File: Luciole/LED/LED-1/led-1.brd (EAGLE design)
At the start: 29.9 x 29.3 mm, 19 parts, among them J1 LiPo, J2 USB-MICROB, Q1 2.5A/30V, U1 MCP73831, U2 3.3V

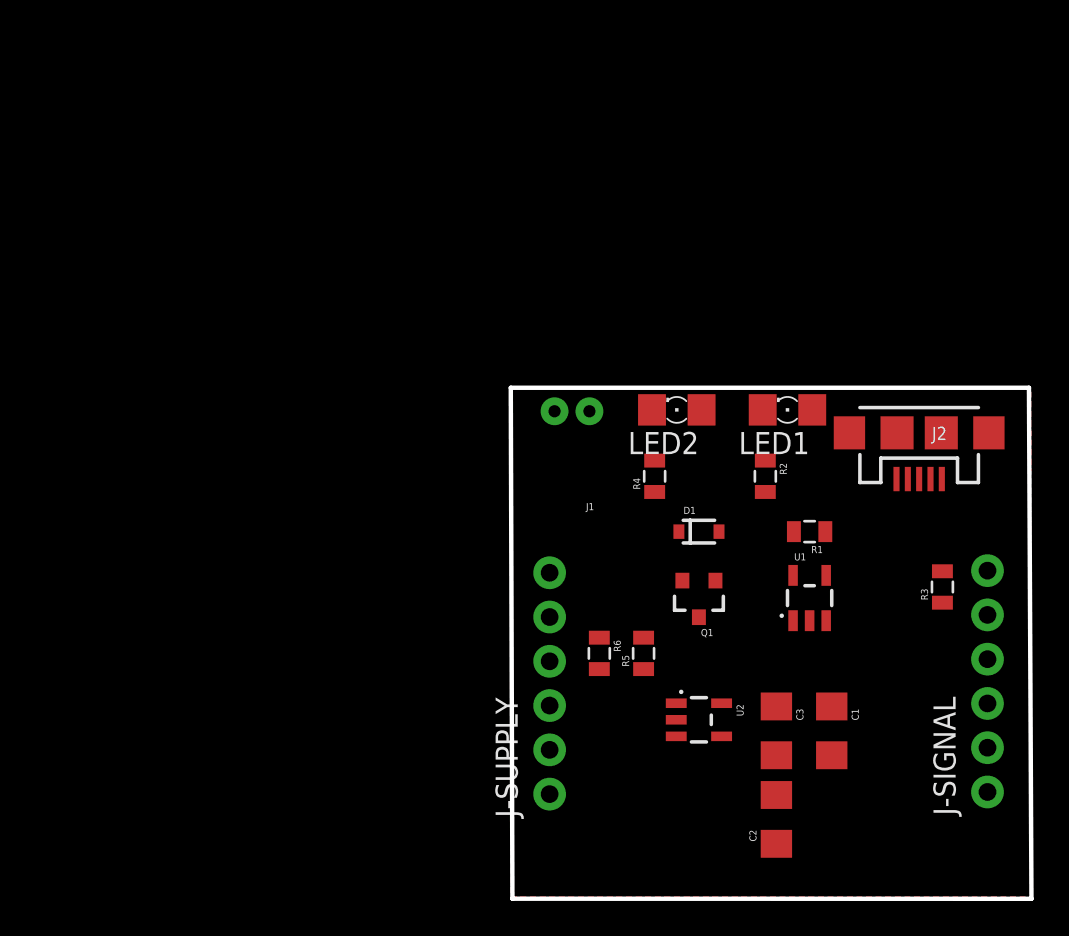
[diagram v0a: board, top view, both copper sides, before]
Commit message: Luciole V1 Ok ; Baballe V1 En cours
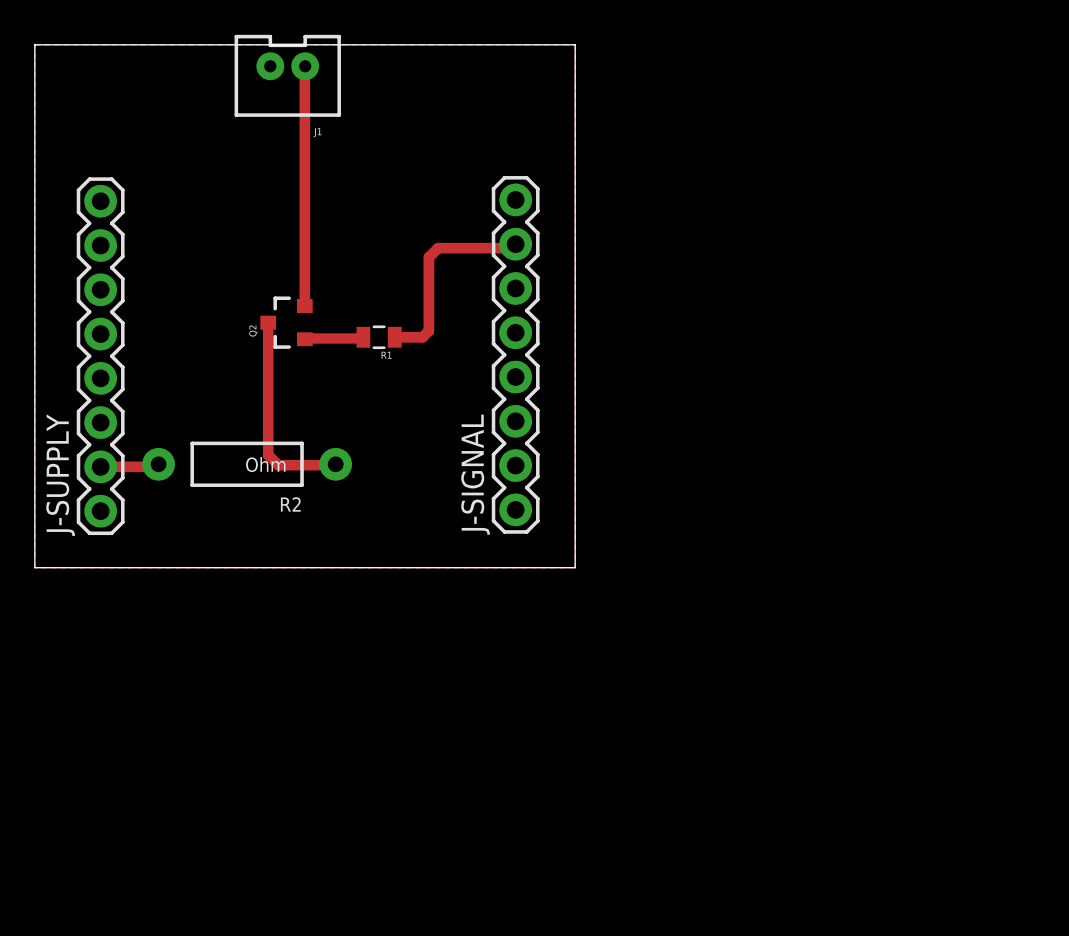
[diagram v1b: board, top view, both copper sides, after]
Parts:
- removed C1: 4.7 uF, SparkFun-Capacitors:1206
- removed C2: 1 uF, SparkFun-Capacitors:1206
- removed C3: 2.2 uF, SparkFun-Capacitors:1206
- removed D1: BAT20J, SparkFun-DiscreteSemi:SOD-323
- removed J2: USB-MICROB, SparkFun-Connectors:USB-MICROB
- removed LED1: JAUNE, eagle-ltspice:LED_1206
- removed LED2: ROUGE, eagle-ltspice:LED_1206
- removed Q1: 2.5A/30V, SparkFun-DiscreteSemi:SOT23-3
- removed R3: 10K, SparkFun-Passives:0805
- removed R4: 200, SparkFun-Passives:0805
- removed R5, R6: 2K, SparkFun-Passives:0805
- removed U1: MCP73831, SparkFun-PowerIC:SOT23-5
- removed U2: 3.3V, SparkFun-PowerIC:SOT23-5
- added Q2: MOSFET-NCHANNELAO3404A, SparkFun-DiscreteSemi:SOT23-3
- J-SIGNAL: value (none) -> J-SIGNAL; device SparkFun-Connectors:1X06_NO_SILK -> SparkFun-Connectors:1X08_ROUND
- J-SUPPLY: value (none) -> J-SUPPLY; device SparkFun-Connectors:1X06_NO_SILK -> SparkFun-Connectors:1X08_ROUND
- J1: value LiPo -> (none); device SparkFun-Connectors:JST-2-PTH-NS -> SparkFun-Connectors:JST-2-PTH-VERT
- R1: value 2K -> 10K
- R2: value ? -> Ohm; device SparkFun-Passives:0805 -> SparkFun-Passives:AXIAL-0.4
- moved J-SIGNAL 31.5 mm to (27.6, 53.3)
- moved J-SUPPLY 30.4 mm to (3.78, 53.2)
- moved R2 29.7 mm to (12.2, 55.9), turned to 180 degrees
- moved R1 27.1 mm to (19.8, 63.2)
- moved J1 25.2 mm to (14.5, 78.2)
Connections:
- removed net N$4: R2.2, U1.1
- removed net N$6: J-SUPPLY.4, R5.1, R6.2
- removed net VUSB: D1.A, J2.VBUS, LED1.A, Q1.1, R3.2, U1.4
- removed net V_BATT: C1.1, J-SUPPLY.5, J1.1, Q1.3, R5.2, U1.3
- new net GPIO12: J-SIGNAL.3
- new net GPIO13: J-SIGNAL.2
- new net GPIO14: J-SIGNAL.4
- new net GPIO16: J-SIGNAL.5
- new net SBUTTON: J-SIGNAL.6
- new net SLED: J-SIGNAL.7, R1.1
- new net VBAT: J-SUPPLY.4
- new net VBAT_MESURE: J-SUPPLY.3
- net GND: no longer C1.2, C2.2, C3.2, J2.GND, J2.MT1, J2.MT2, LED2.C, R1.1, R3.1, R6.1, U1.2, U2.2, U2.4
- net N$1: now also J1.1, Q2.2; no longer LED1.C, R2.1
- net N$2: now also Q2.1; no longer U1.5
- net N$3: now also Q2.3, R2.P$1; no longer LED2.A, R4.1
- net VCC: now also J-SUPPLY.5; no longer C3.1, J-SUPPLY.6, R4.2, U2.5
- net VIN: now also J-SUPPLY.2, R2.P$2; no longer C2.1, D1.C, J-SUPPLY.3, Q1.2, U2.1, U2.3
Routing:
- net N$1: track 0.00 -> 13.8 mm
- net N$3: track 0.00 -> 11.7 mm
- net SLED: track 0.00 -> 11.6 mm
- net N$2: track 0.00 -> 3.52 mm
- net VIN: track 0.00 -> 3.38 mm
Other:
- board size 29.9 x 29.3 mm -> 31 x 30 mm

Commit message: V2 de la Baballe
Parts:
- R2: value Ohm -> (none); device SparkFun-Passives:AXIAL-0.4 -> SparkFun-Passives:AXIAL-0.5
- moved J1 10.2 mm to (4.35, 77.0)
- moved R1 5.68 mm to (22.3, 68.3)
- moved R2 4.50 mm to (16.5, 57.1)
- moved Q2 4.40 mm to (10.9, 66.6), turned to 180 degrees
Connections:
- net GND: now also R2.P$1; no longer J1.2
- net N$1: now also R2.P$2; no longer J1.1
- net N$3: now also J1.2; no longer R2.P$1
- net VIN: now also J1.1; no longer R2.P$2
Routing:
- net N$1: track 13.8 -> 0.00 mm
- net N$3: track 11.7 -> 0.00 mm
- net SLED: track 11.6 -> 0.00 mm
- net N$2: track 3.52 -> 0.00 mm
- net VIN: track 3.38 -> 0.00 mm
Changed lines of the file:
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@@
 <param name="RoutingGrid" value="50mil"/>
 <param name="AutoGrid" value="1"/>
-<param name="Efforts" value="0"/>
+<param name="Efforts" value="2"/>
 <param name="TopRouterVariant" value="1"/>
 <param name="tpViaShape" value="round"/>
@@
 <attribute name="PROD_ID" value="CONN-08437" x="3.775225" y="53.245359375" size="1.778" layer="27" rot="R90" display="off"/>
 </element>
-<element name="J1" library="SparkFun-Connectors" package="JST-2-PTH-VERT" value="" x="14.51" y="78.22" rot="R180"/>
-<element name="Q2" library="SparkFun-DiscreteSemi" package="SOT23-3" value="MOSFET-NCHANNELAO3404A" x="14.49" y="64.06" rot="R90">
-<attribute name="PROD_ID" value="TRAN-12988" x="14.49" y="64.06" size="1.778" layer="27" rot="R90" display="off"/>
+<element name="J1" library="SparkFun-Connectors" package="JST-2-PTH-VERT" value="" x="4.35" y="76.95" rot="R180"/>
+<element name="Q2" library="SparkFun-DiscreteSemi" package="SOT23-3" value="MOSFET-NCHANNELAO3404A" x="10.87" y="66.56" rot="R180">
+<attribute name="PROD_ID" value="TRAN-12988" x="10.87" y="66.56" size="1.778" layer="27" rot="R180" display="off"/>
 </element>
-<element name="R1" library="SparkFun-Passives" package="0805" value="10K" x="19.75" y="63.22" rot="R180"/>
-<element name="R2" library="SparkFun-Passives" package="AXIAL-0.4" value="Ohm" x="12.178065625" y="55.933590625" rot="R180"/>
+<element name="R1" library="SparkFun-Passives" package="0805" value="10K" x="22.29" y="68.3" rot="R180"/>
+<element name="R2" library="SparkFun-Passives" package="AXIAL-0.5" value="" x="16.51" y="57.15" rot="R180"/>
 </elements>
 <signals>
-<signal name="GND">
+<signal name="GND" class="2">
 <contactref element="J-SIGNAL" pad="1"/>
 <contactref element="J-SUPPLY" pad="1"/>
-<contactref element="J1" pad="2"/>
 <polygon width="0.4064" layer="1" isolate="0.4064" orphans="yes">
 <vertex x="0" y="80"/>
@@
 <vertex x="0" y="50"/>
 </polygon>
+<contactref element="R2" pad="P$1"/>
 </signal>
 <signal name="VCC" class="2">
@@
 <signal name="VIN" class="2">
 <contactref element="J-SUPPLY" pad="2"/>
-<contactref element="R2" pad="P$2"/>
-<wire x1="3.775225" y1="55.785359375" x2="6.949834375" y2="55.785359375" width="0.6096" layer="1"/>
-<wire x1="6.949834375" y1="55.785359375" x2="7.098065625" y2="55.933590625" width="0.6096" layer="1"/>
+<contactref element="J1" pad="1"/>
+<wire x1="3.775225" y1="55.785359375" x2="5.35" y2="77.5" width="0" layer="19" extent="1-1"/>
 </signal>
 <signal name="VBAT" class="2">
@@
 <contactref element="J-SIGNAL" pad="7"/>
 <contactref element="R1" pad="1"/>
-<wire x1="20.65" y1="63.22" x2="22.24146875" y2="63.22" width="0.6096" layer="1"/>
-<wire x1="22.24146875" y1="63.22" x2="22.608228125" y2="63.586759375" width="0.6096" layer="1"/>
-<wire x1="22.608228125" y1="63.586759375" x2="22.608228125" y2="67.809184375" width="0.6096" layer="1"/>
-<wire x1="22.608228125" y1="67.809184375" x2="23.135021875" y2="68.335978125" width="0.6096" layer="1"/>
-<wire x1="23.135021875" y1="68.335978125" x2="27.3606875" y2="68.335978125" width="0.6096" layer="1"/>
-<wire x1="27.3606875" y1="68.335978125" x2="27.585096875" y2="68.5603875" width="0.6096" layer="1"/>
+<wire x1="27.585096875" y1="68.5603875" x2="23.19" y2="68.3" width="0" layer="19" extent="1-1"/>
 </signal>
 <signal name="SBUTTON">
@@
 <contactref element="R1" pad="2"/>
 <contactref element="Q2" pad="1"/>
-<wire x1="15.5992" y1="63.1516" x2="15.49" y2="63.11" width="0.3" layer="1"/>
-<wire x1="18.7442" y1="63.1516" x2="18.85" y2="63.22" width="0.3" layer="1"/>
-<wire x1="15.5992" y1="63.1516" x2="18.7816" y2="63.1516" width="0.6096" layer="1"/>
-<wire x1="18.7816" y1="63.1516" x2="18.85" y2="63.22" width="0.6096" layer="1"/>
+<wire x1="11.82" y1="67.56" x2="21.39" y2="68.3" width="0" layer="19" extent="1-1"/>
 </signal>
-<signal name="N$1">
+<signal name="N$1" class="2">
 <contactref element="Q2" pad="2"/>
-<contactref element="J1" pad="1"/>
-<wire x1="15.49" y1="65.01" x2="15.49" y2="78.75" width="0.6096" layer="1"/>
-<wire x1="15.49" y1="78.75" x2="15.51" y2="78.77" width="0.6096" layer="1"/>
+<contactref element="R2" pad="P$2"/>
+<wire x1="10.16" y1="57.15" x2="9.92" y2="67.56" width="0" layer="19" extent="1-1"/>
 </signal>
-<signal name="N$3">
-<contactref element="R2" pad="P$1"/>
+<signal name="N$3" class="2">
 <contactref element="Q2" pad="3"/>
-<wire x1="13.39" y1="64.06" x2="13.39" y2="56.46" width="0.6096" layer="1"/>
-<wire x1="13.39" y1="56.46" x2="13.97" y2="55.88" width="0.6096" layer="1"/>
-<wire x1="13.97" y1="55.88" x2="17.204475" y2="55.88" width="0.6096" layer="1"/>
-<wire x1="17.204475" y1="55.88" x2="17.258065625" y2="55.933590625" width="0.6096" layer="1"/>
+<contactref element="J1" pad="2"/>
+<wire x1="3.35" y1="77.5" x2="10.87" y2="65.46" width="0" layer="19" extent="1-1"/>
 </signal>
 </signals>
